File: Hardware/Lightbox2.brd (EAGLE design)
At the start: 52 x 54.3 mm, 12 parts, among them IC1 7805T, U1 328P

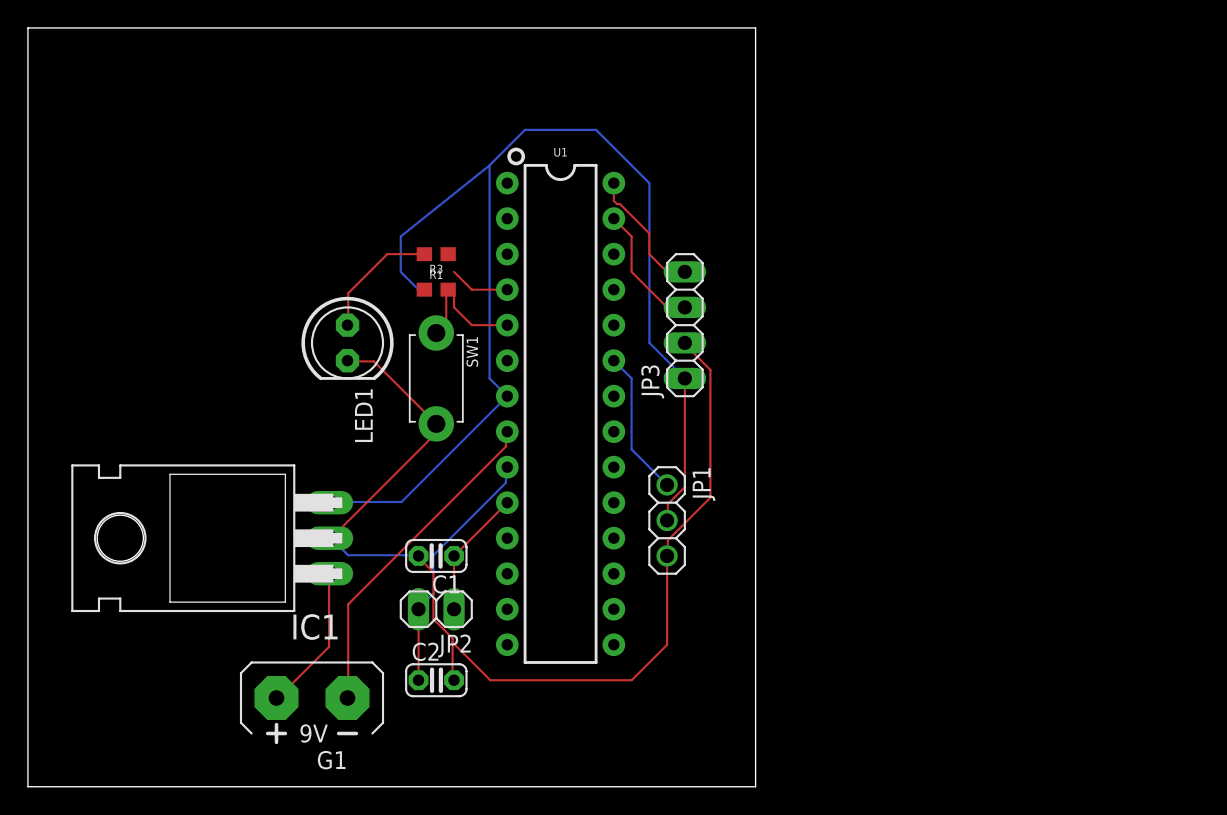
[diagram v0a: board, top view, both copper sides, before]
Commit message: Increase trace thickness and replace wrong components
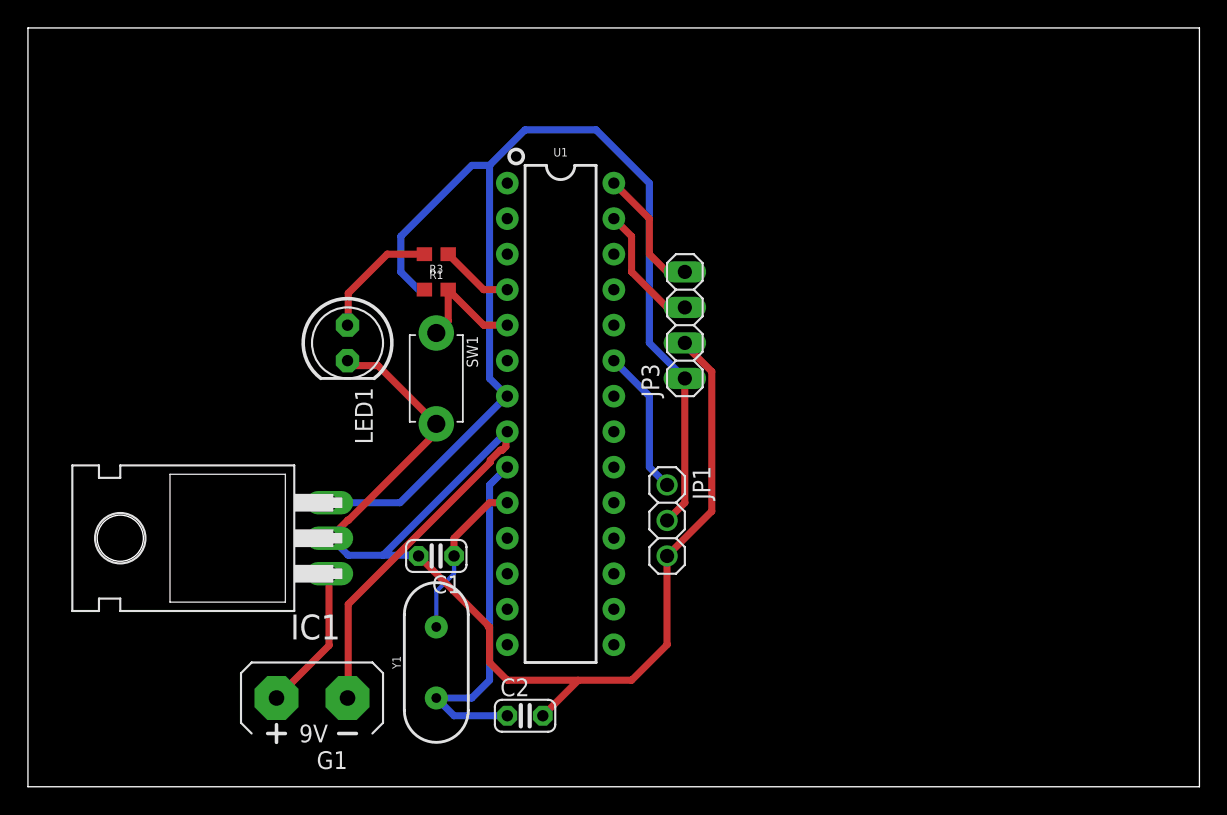
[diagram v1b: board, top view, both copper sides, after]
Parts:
- removed JP2: (no value), pinhead:1X02
- added Y1: 16MHz, SparkFun-Clocks:HC49US
- R1: value 150 -> 10k
- moved C2 6.84 mm to (35.6, 5.08)
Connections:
- net XTAL1: now also Y1.1; no longer JP2.2
- net XTAL2: now also Y1.2; no longer JP2.1
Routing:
- net GND: track 101.5 -> 131.7 mm
- net XTAL1: track 17.9 -> 25.7 mm
- net XTAL2: track 9.35 -> 11.7 mm
- net PD2: track 4.34 -> 5.28 mm
- net PD3: track 9.31 -> 8.73 mm
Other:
- board size 52 x 54.3 mm -> 83.8 x 54.3 mm

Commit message: Add dimensions and replace battery with 2pin header
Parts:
- removed G1: AB9V, battery:AB9V
- added JP2: (no value), pinhead:1X02
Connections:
- net 9V: now also JP2.2; no longer G1.+
- net GND: now also JP2.1; no longer G1.-
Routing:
- net GND: track 131.7 -> 134.7 mm
- net 9V: track 10.5 -> 8.15 mm
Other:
- board size 83.8 x 54.3 mm -> 52 x 49.2 mm
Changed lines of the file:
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@@
 <layer number="43" name="vRestrict" color="2" fill="10" visible="yes" active="yes"/>
 <layer number="44" name="Drills" color="7" fill="1" visible="no" active="yes"/>
-<layer number="45" name="Holes" color="7" fill="1" visible="no" active="yes"/>
+<layer number="45" name="Holes" color="7" fill="1" visible="yes" active="yes"/>
 <layer number="46" name="Milling" color="3" fill="1" visible="no" active="yes"/>
 <layer number="47" name="Measures" color="7" fill="1" visible="no" active="yes"/>
@@
 <board>
 <plain>
-<wire x1="0" y1="0" x2="83.8" y2="0" width="0" layer="20"/>
-<wire x1="83.8" y1="0" x2="83.8" y2="54.28" width="0" layer="20"/>
-<wire x1="83.8" y1="54.28" x2="0" y2="54.28" width="0" layer="20"/>
-<wire x1="0" y1="54.28" x2="0" y2="0" width="0" layer="20"/>
+<wire x1="0" y1="0" x2="52.05" y2="0" width="0" layer="20"/>
+<wire x1="52.05" y1="0" x2="52.05" y2="49.2" width="0" layer="20"/>
+<wire x1="52.05" y1="49.2" x2="0" y2="49.2" width="0" layer="20"/>
+<wire x1="0" y1="49.2" x2="0" y2="0" width="0" layer="20"/>
+<dimension x1="0" y1="0" x2="52.05" y2="0" x3="26.025" y3="-5.08" textsize="1.778" layer="1"/>
+<dimension x1="0" y1="54.28" x2="0" y2="0" x3="-10.16" y3="27.14" textsize="1.778" layer="1"/>
+<dimension x1="0" y1="49.2" x2="0" y2="0" x3="-5.08" y3="24.6" textsize="1.778" layer="1"/>
+<dimension x1="46.99" y1="29.21" x2="45.72" y2="21.59" x3="58.42" y3="25.4" textsize="1.778" layer="1" dtype="vertical"/>
 </plain>
 <attributes>
@@
 <attribute name="VALUE" x="33.782" y="2.413" size="1.27" layer="27" ratio="10"/>
 </element>
-<element name="G1" library="battery" library_urn="urn:adsk.eagle:library:109" package="AB9V" package3d_urn="urn:adsk.eagle:package:4600/1" value="AB9V" x="20.32" y="6.35" rot="R90">
-<attribute name="NAME" x="22.86" y="2.54" size="1.27" layer="25" ratio="10" rot="R180"/>
-<attribute name="VALUE" x="22.86" y="10.795" size="1.27" layer="27" ratio="10" rot="R180"/>
-</element>
 <element name="IC1" library="adafruit" library_urn="urn:adsk.eagle:library:420" package="TO220H" package3d_urn="urn:adsk.eagle:package:6240670/1" value="7805T" x="11.43" y="17.78" rot="R90">
 <attribute name="NAME" x="22.352" y="12.319" size="1.778" layer="25" ratio="10" rot="R180"/>
@@
 <attribute name="PROD_ID" value="RES-00824" x="29.21" y="35.56" size="1.778" layer="27" display="off"/>
 <attribute name="VALUE" x="29.21" y="34.798" size="0.6096" layer="27" font="vector" ratio="20" align="top-center"/>
+</element>
+<element name="JP2" library="pinhead" library_urn="urn:adsk.eagle:library:325" package="1X02" package3d_urn="urn:adsk.eagle:package:22435/2" value="" x="20.32" y="6.35" rot="R90">
+<attribute name="NAME" x="18.4912" y="3.7338" size="1.27" layer="25" ratio="10" rot="R90"/>
+<attribute name="VALUE" x="23.495" y="3.81" size="1.27" layer="27" rot="R90"/>
 </element>
 </elements>
@@
 <wire x1="25.0444" y1="30.1244" x2="29.1592" y2="26.0096" width="0.1524" layer="1"/>
 <wire x1="29.21" y1="25.96" x2="29.1592" y2="26.0096" width="0.1524" layer="1"/>
-<contactref element="G1" pad="-"/>
 <contactref element="U1" pad="8"/>
 <wire x1="25.4" y1="16.5608" x2="27.94" y2="16.5608" width="0.1524" layer="16"/>
@@
 <wire x1="27.8892" y1="16.5608" x2="27.94" y2="16.51" width="0.508" layer="16"/>
 <wire x1="33.02" y1="11.43" x2="27.94" y2="16.51" width="0.508" layer="1"/>
-<wire x1="22.86" y1="6.35" x2="22.9108" y2="6.4008" width="0.508" layer="1"/>
 <wire x1="22.9108" y1="6.4008" x2="22.9108" y2="13.0556" width="0.508" layer="1"/>
 <wire x1="34.1884" y1="24.3332" x2="34.1884" y2="25.4" width="0.508" layer="1"/>
@@
 <wire x1="25.4" y1="16.5608" x2="34.2392" y2="25.4" width="0.508" layer="16"/>
 <wire x1="34.2392" y1="25.4" x2="34.29" y2="25.4" width="0.508" layer="16"/>
-</signal>
-<signal name="9V">
-<contactref element="G1" pad="+"/>
-<contactref element="IC1" pad="1"/>
-<wire x1="21.5392" y1="15.1892" x2="21.59" y2="15.24" width="0.508" layer="1"/>
-<wire x1="17.78" y1="6.35" x2="21.5392" y2="10.1092" width="0.508" layer="1"/>
-<wire x1="21.5392" y1="10.1092" x2="21.5392" y2="15.1892" width="0.508" layer="1"/>
+<contactref element="JP2" pad="1"/>
+<wire x1="20.32" y1="5.08" x2="21.59" y2="5.08" width="0.508" layer="1"/>
+<wire x1="21.59" y1="5.08" x2="22.9108" y2="6.4008" width="0.508" layer="1"/>
 </signal>
 <signal name="VCC">
@@
 <wire x1="33.02" y1="20.32" x2="34.29" y2="20.32" width="0.508" layer="1"/>
 </signal>
+<signal name="9V">
+<contactref element="JP2" pad="2"/>
+<contactref element="IC1" pad="1"/>
+<wire x1="20.32" y1="7.62" x2="21.59" y2="8.89" width="0.508" layer="1"/>
+<wire x1="21.59" y1="8.89" x2="21.59" y2="15.24" width="0.508" layer="1"/>
+</signal>
 </signals>

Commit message: Schematic and PCB design for final review
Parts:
- removed R1: 10k, SparkFun-Resistors:0603
- added R2: (no value), adafruit:0204/5
- added SWITCH: (no value), pinhead:1X02
- moved LED1 2.54 mm to (22.9, 34.3)
- moved R3 2.54 mm to (29.2, 35.6)
- renumbered JP1 to PULSESENSOR, JP2 to BATTERY, JP3 to LCD
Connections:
- net 9V: now also SWITCH.1, SWITCH.2
- net PD3: now also R2.2; no longer R1.2
- net VCC: now also R2.1; no longer R1.1
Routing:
- net 9V: track 8.15 -> 17.9 mm
- net VCC: track 85.5 -> 76.3 mm
- net PD3: track 8.73 -> 12.3 mm
- net N$6: track 8.91 -> 5.50 mm
- net GND: track 134.7 -> 136.2 mm
- net PD2: track 5.28 -> 4.23 mm
